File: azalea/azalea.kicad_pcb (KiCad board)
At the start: 4 copper layers, 70.6 x 53.3 mm, 103 parts, among them J1 NEIGHBOR1, J2 NEIGHBOR2, J3 USB-MICRO-B-SHIELDED, J4 USB-MICRO-B-SHIELDED, J5 JTAG, J6 POWER, J7 BONUS_ROW, SW1 DFU, SW2 RESET, U1 LPC4330FBD144, U2 W25Q16DV, U3 AP7333, U4 IP4220CZ6, U5 AP2553W6-7, X1 MCU_XTAL, X2 RTC_XTAL

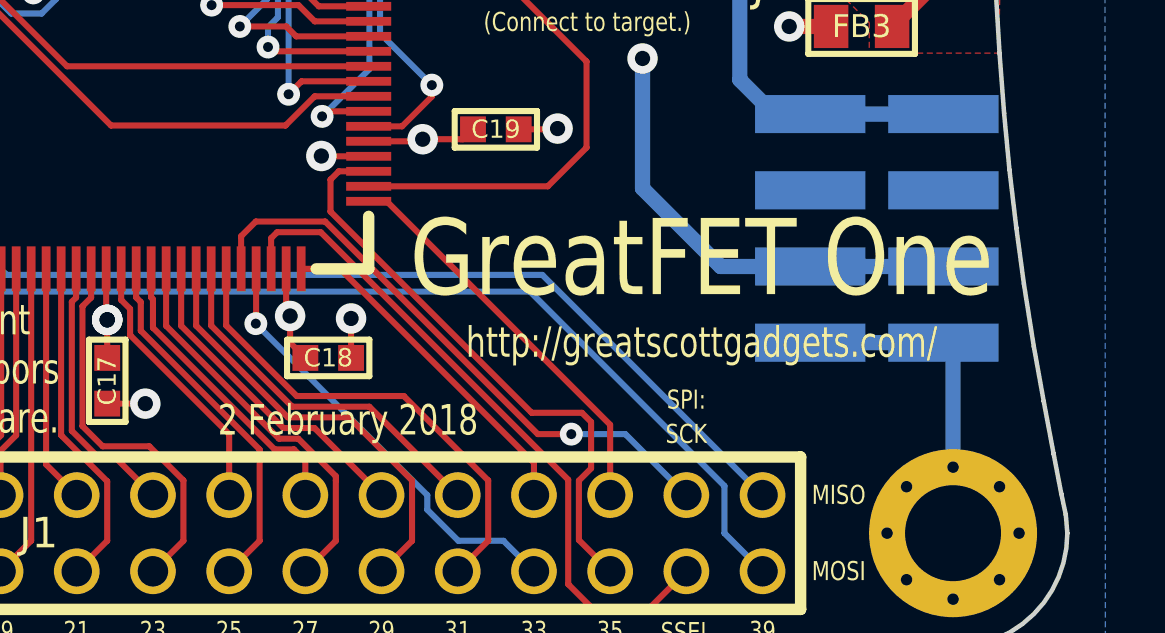
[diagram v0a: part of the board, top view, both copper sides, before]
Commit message: Renamed GreatFET One back to Azalea. The name GreatFET One will be used only for boards marketed by Great Scott Gadgets. Azalea should be used to refer to other boards of the same design.
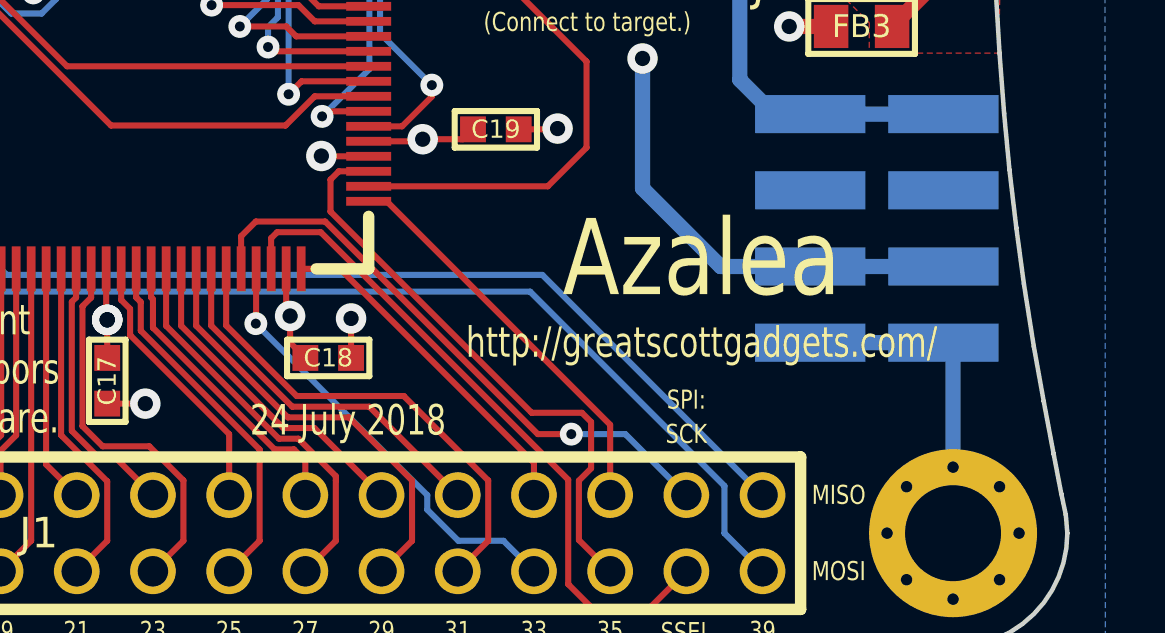
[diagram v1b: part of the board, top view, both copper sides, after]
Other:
- board text added: "24 July 2018"
- board text added: "Azalea"
- board text removed: "2 February 2018"
- board text removed: "GreatFET One"
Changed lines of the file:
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@@
     (links 387)
     (no_connects 0)
-    (area 105.842999 71.044999 176.605001 124.535001)
+    (area 93.424104 68.58 207.466001 127.000001)
     (thickness 1.6)
     (drawings 230)
@@
   )
   (page A4)
+  (title_block
+    (title Azalea)
+    (date 2018-07-24)
+    (company "Copyright 2015-2018 Great Scott Gadgets")
+    (comment 1 "License: BSD-3-Clause")
+    (comment 2 http://greatscottgadgets.com/greatfet/)
+  )
   (layers
     (0 F.Cu signal)
@@
   (gr_line (start 128.778 81.026) (end 128.27 81.534) (angle 90) (layer F.SilkS) (width 0.15))
   (gr_arc (start 126.238 81.026) (end 128.778 81.026) (angle 150) (layer F.SilkS) (width 0.2032))
-  (gr_text "2 February 2018" (at 152.5524 116.8908) (layer F.SilkS)
+  (gr_text "24 July 2018" (at 152.5524 116.8908) (layer F.SilkS)
     (effects (font (size 1.016 0.762) (thickness 0.1524)))
   )
@@
   (gr_arc (start 112.3188 74.93) (end 112.3188 71.12) (angle -70) (layer Cmts.User) (width 0.15))
   (gr_arc (start 172.72 120.65) (end 176.53 120.65) (angle 90) (layer Edge.Cuts) (width 0.15))
-  (gr_text "GreatFET One" (at 164.338 111.506) (layer F.SilkS)
+  (gr_text Azalea (at 164.338 111.506) (layer F.SilkS)
     (effects (font (size 2.54 2.032) (thickness 0.381)))
   )

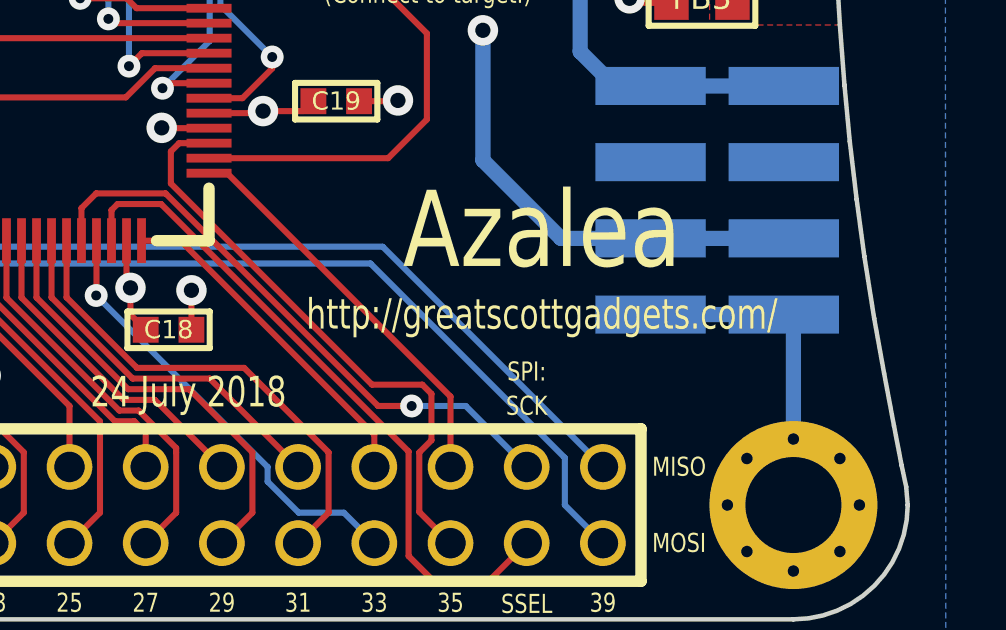
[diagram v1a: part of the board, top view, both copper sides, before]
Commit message: Azalea: updated URL on silkcreen, adding greatfet and changing the protocol to https
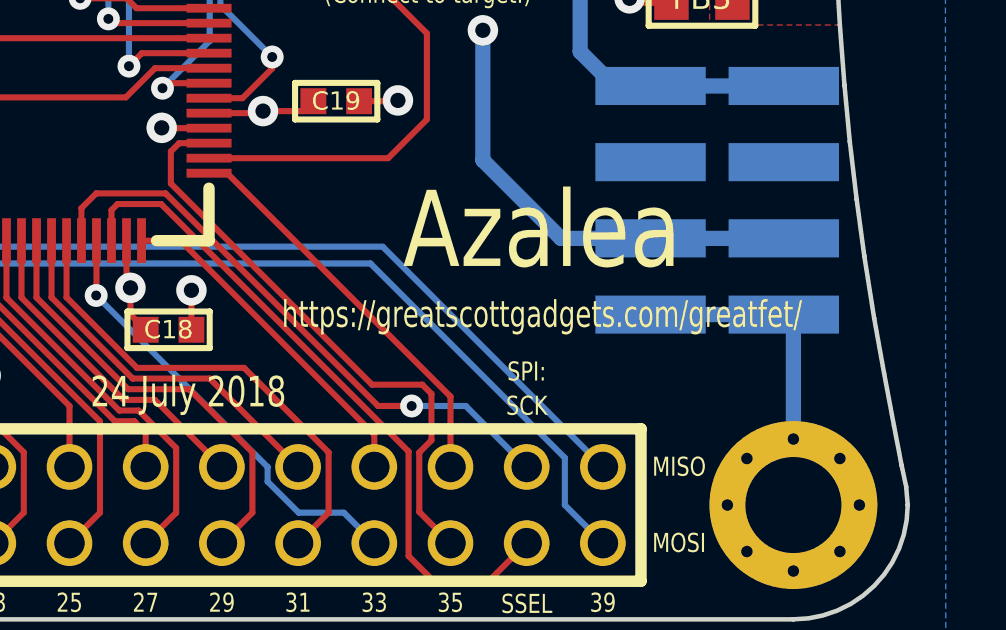
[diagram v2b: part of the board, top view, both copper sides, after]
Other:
- board text added: "https://greatscottgadgets.com/greatfet/"
- board text removed: "http://greatscottgadgets.com/"
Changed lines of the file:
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@@
     (effects (font (size 1.016 0.762) (thickness 0.1524)))
   )
-  (gr_text http://greatscottgadgets.com/ (at 164.338 114.3) (layer F.SilkS)
-    (effects (font (size 1.016 0.762) (thickness 0.1524)))
+  (gr_text https://greatscottgadgets.com/greatfet/ (at 164.338 114.3) (layer F.SilkS)
+    (effects (font (size 0.889 0.635) (thickness 0.127)))
   )
   (gr_text J5 (at 122.428 113.411) (layer F.SilkS)
